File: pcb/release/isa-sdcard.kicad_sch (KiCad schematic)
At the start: 47 parts, among them J1 SDCARD, J2 Bus_ISA_8bit_AB_Rev0, SW1 ADDR SEL, U1 74HC00, U10 74HC74, U11 74HC08, U12 74HC04, U13 74HC74, U2 74HCT32, U3 74HCT139, U4 74HC163, U5 74HC00, U6 74HC165, U7 74HC595, U8 74HCT688, U9 74HCT245, X1 16MHz

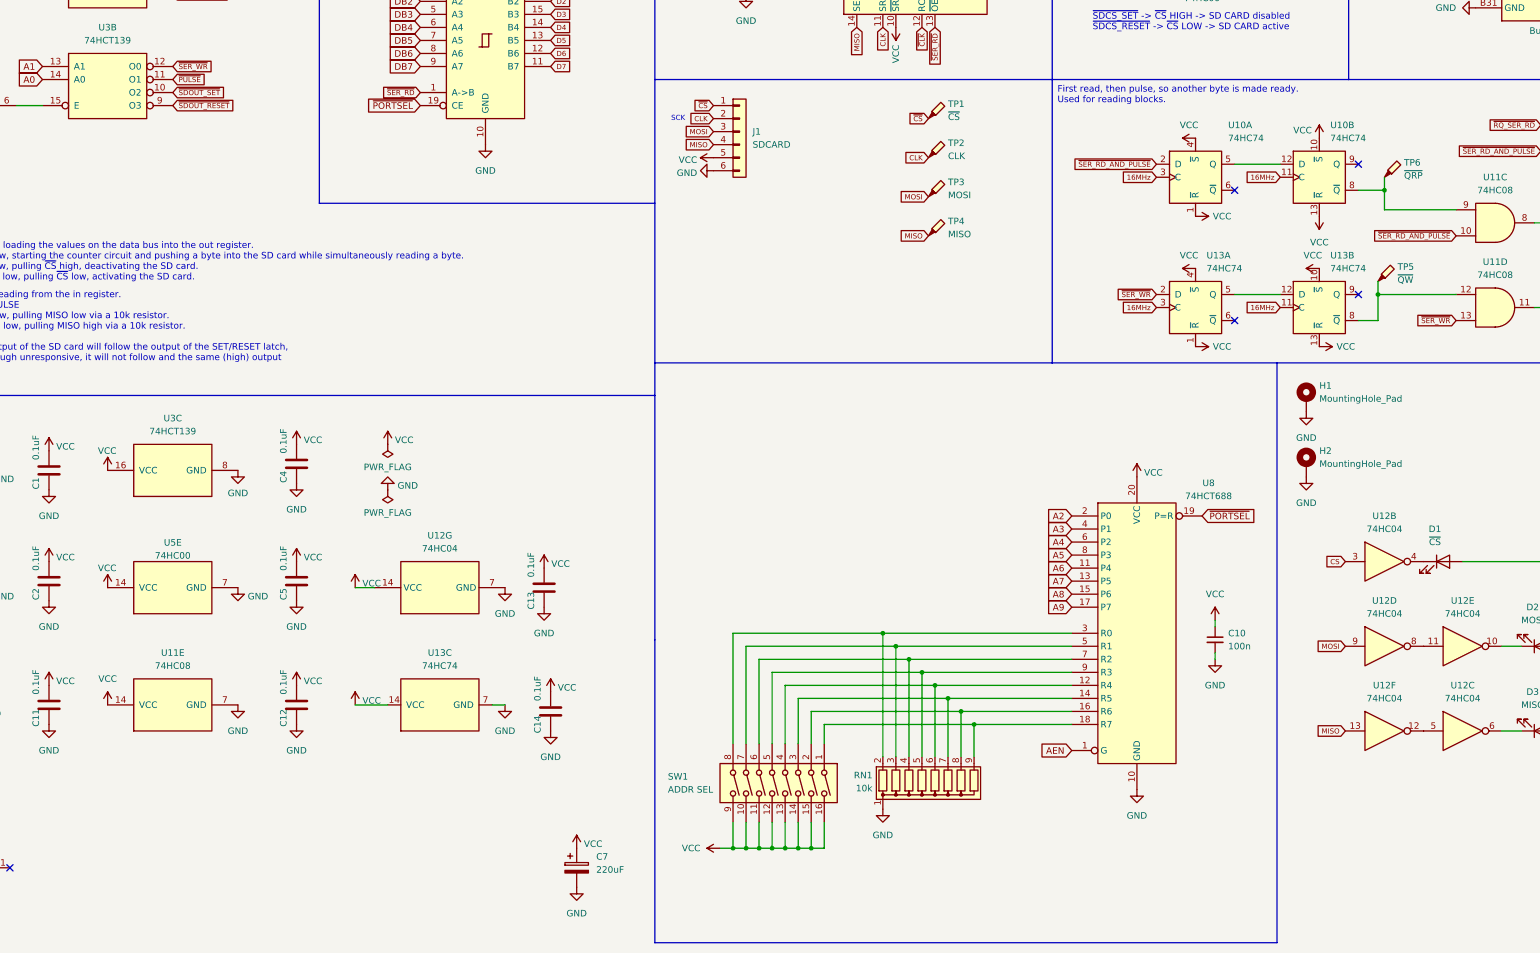
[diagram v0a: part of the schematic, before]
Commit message: Adding PCB variant
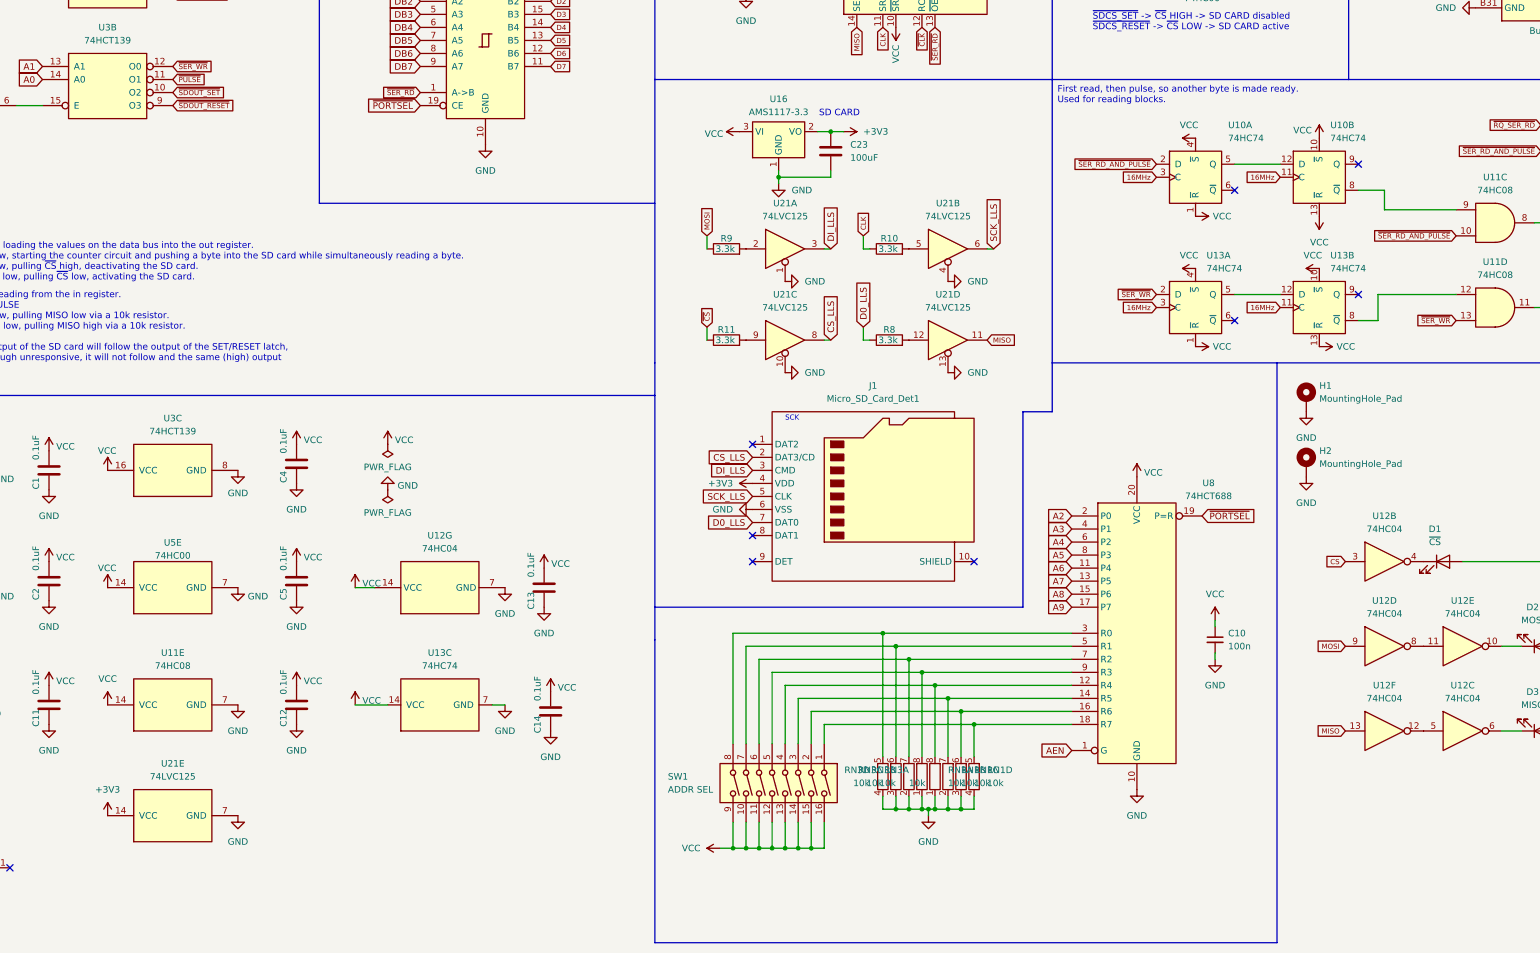
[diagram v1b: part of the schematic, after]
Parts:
- removed C7: 220uF, Capacitor_THT:CP_Radial_D6.3mm_P2.50mm, symbol Device:C_Polarized
- removed J1: SDCARD, sdcard-holder:sdcard-socket, symbol Connector_Generic:Conn_01x06
- removed RN1: 10k, Resistor_THT:R_Array_SIP9, symbol Device:R_Network08
- removed TP1: ~{CS}, TestPoint:TestPoint_Loop_D2.54mm_Drill1.5mm_Beaded, symbol Connector:TestPoint_Probe
- removed TP2: CLK, TestPoint:TestPoint_Loop_D2.54mm_Drill1.5mm_Beaded, symbol Connector:TestPoint_Probe
- removed TP3: MOSI, TestPoint:TestPoint_Loop_D2.54mm_Drill1.5mm_Beaded, symbol Connector:TestPoint_Probe
- removed TP4: MISO, TestPoint:TestPoint_Loop_D2.54mm_Drill1.5mm_Beaded, symbol Connector:TestPoint_Probe
- removed TP5: ~{QW}, TestPoint:TestPoint_Loop_D2.54mm_Drill1.5mm_Beaded, symbol Connector:TestPoint_Probe
- removed TP6: ~{QRP}, TestPoint:TestPoint_Loop_D2.54mm_Drill1.5mm_Beaded, symbol Connector:TestPoint_Probe
- added C23: 100uF, Capacitor_SMD:C_1206_3216Metric_Pad1.33x1.80mm_HandSolder, symbol Device:C
- added J1: Micro_SD_Card_Det1, components:CONN9_MSD-1_CUD, symbol Connector:Micro_SD_Card_Det1
- added R10, R11, R8, R9: 3.3k, Resistor_SMD:R_0805_2012Metric_Pad1.20x1.40mm_HandSolder, symbol Device:R
- added RN1, RN3: 10k, Resistor_SMD:R_Array_Convex_4x0612, symbol Device:R_Pack04_Split
- added U16: AMS1117-3.3, Package_TO_SOT_SMD:SOT-223-3_TabPin2, symbol Regulator_Linear:AMS1117-3.3
- added U21: 74LVC125, Package_SO:TSSOP-14_4.4x5mm_P0.65mm, symbol 74xx:74LVC125
- C1, C10, C11, C12, C13, C14, C2, C3, C4, C5, C6, C8, C9: footprint Capacitor_THT:C_Disc_D5.0mm_W2.5mm_P5.00mm -> Capacitor_SMD:C_0805_2012Metric
- D1, D2, D3: footprint LED_THT:LED_D5.0mm -> LED_SMD:LED_0805_2012Metric
- R1, R2, R3, R4: footprint Resistor_THT:R_Axial_DIN0207_L6.3mm_D2.5mm_P7.62mm_Horizontal -> Resistor_SMD:R_0805_2012Metric
- U1, U10, U11, U12, U13, U2, U5: footprint Package_DIP:DIP-14_W7.62mm_Socket -> Package_SO:SOIC-14_3.9x8.7mm_P1.27mm
- U3, U4, U6, U7: footprint Package_DIP:DIP-16_W7.62mm_Socket -> Package_SO:SOIC-16_3.9x9.9mm_P1.27mm
- U8, U9: footprint Package_DIP:DIP-20_W7.62mm_Socket -> Package_SO:SOIC-20W_7.5x12.8mm_P1.27mm
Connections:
- net CLK: now also R10.1
- net GND: now also C23.2, J1.6 (VSS), RN1.1 (R1.1), RN1.2 (R2.1), RN1.3 (R3.1), RN1.4 (R4.1), RN3.1 (R1.1), RN3.2 (R2.1), RN3.3 (R3.1), RN3.4 (R4.1), U16.1 (GND), U21.1, U21.10, U21.13, U21.4, U21.7 (GND)
- net MISO: now also U21.11
- net MOSI: now also R9.1
- net VCC: now also U16.3 (VI)
- net ~{CS}: now also R11.1
- net at SW1.1, U8.18 (R7): now also RN1.5 (R4.2)
- net at SW1.2, U8.16 (R6): now also RN1.6 (R3.2)
- net at SW1.3, U8.14 (R5): now also RN1.7 (R2.2)
- net at SW1.4, U8.12 (R4): now also RN1.8 (R1.2)
- net at SW1.5, U8.9 (R3): now also RN3.8 (R1.2)
- net at SW1.6, U8.7 (R2): now also RN3.7 (R2.2)
- net at SW1.7, U8.5 (R1): now also RN3.6 (R3.2)
- net at SW1.8, U8.3 (R0): now also RN3.5 (R4.2)
- new net: R11.2, U21.9
- new net: R10.2, U21.5
- new net: R8.2, U21.12
- new net: R9.2, U21.2
- new net +3V3: C23.1, J1.4 (VDD), U16.2 (VO), U21.14 (VCC)
- new net CS_LLS: J1.2 (DAT3/CD), U21.8
- new net D0_LLS: J1.7 (DAT0), R8.1
- new net DI_LLS: J1.3 (CMD), U21.3
- new net SCK_LLS: J1.5 (CLK), U21.6
- no-connect marks 46 -> 50
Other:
- note added: "SD CARD"

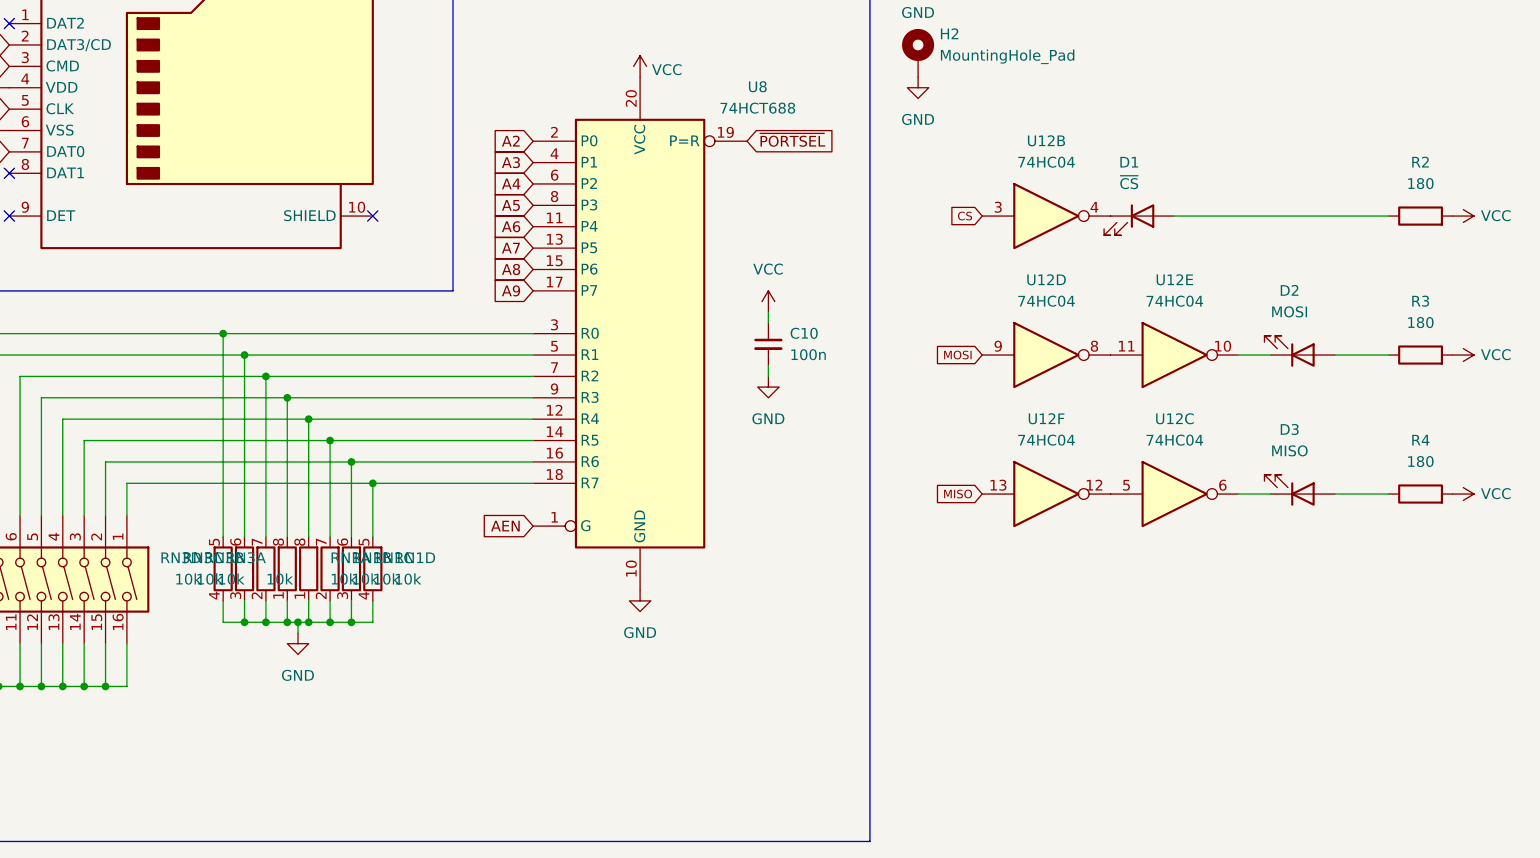
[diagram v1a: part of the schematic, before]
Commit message: Fixing CS bug in code, adding logos to PCB
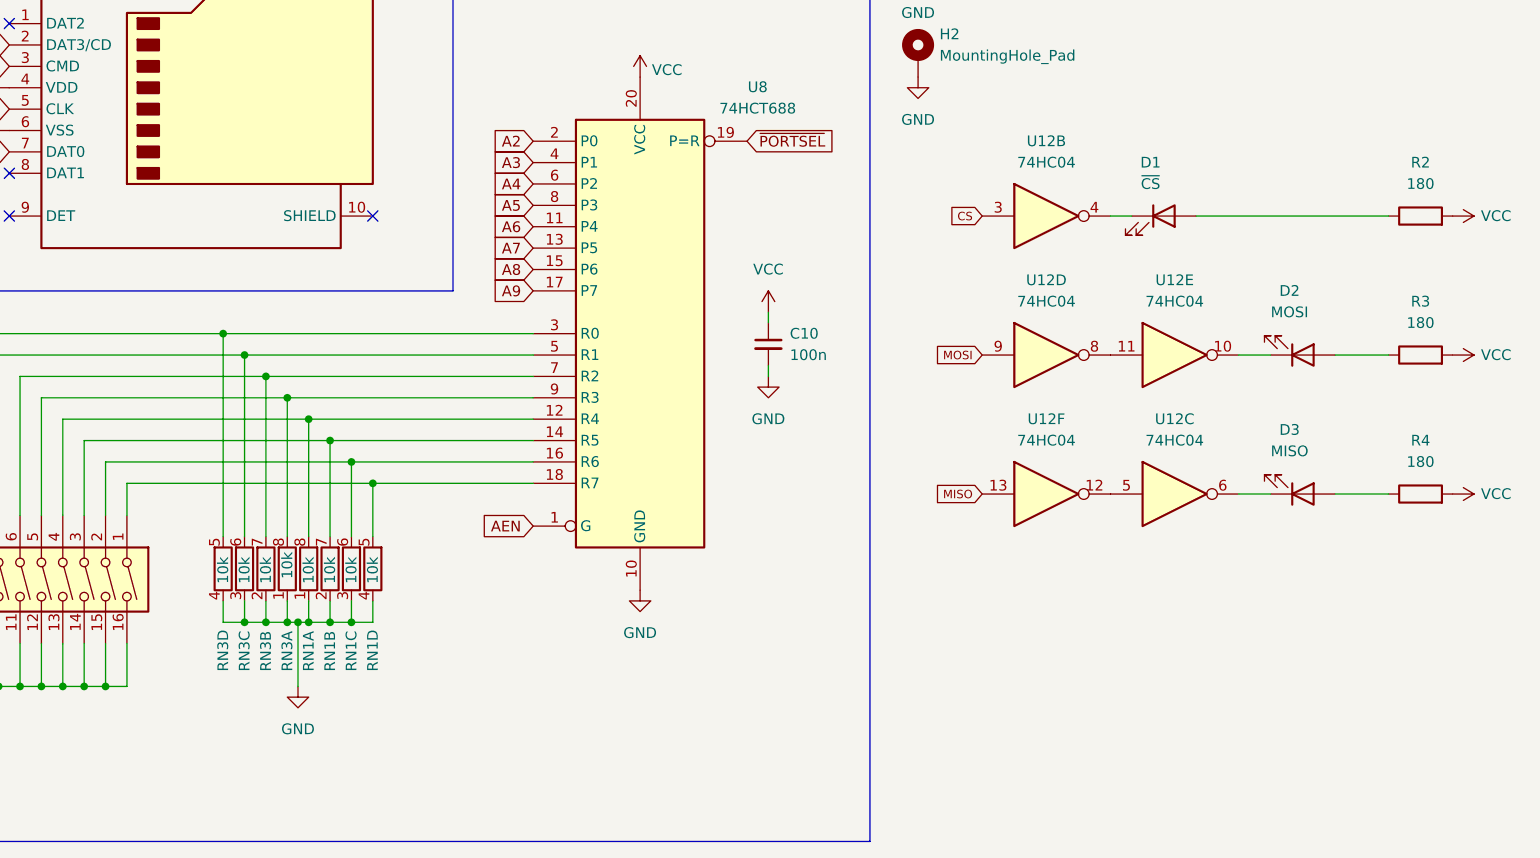
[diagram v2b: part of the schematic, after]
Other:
- moved on the sheet: D1
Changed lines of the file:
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@@
 	(wire
 		(pts
-			(xy 228.6 259.08) (xy 228.6 257.81)
+			(xy 228.6 265.43) (xy 228.6 257.81)
 		)
 		(stroke
@@
 	(wire
 		(pts
+			(xy 327.66 209.55) (xy 325.12 209.55)
+		)
+		(stroke
+			(width 0)
+			(type default)
+		)
+	)
+	(wire
+		(pts
 			(xy 209.55 166.37) (xy 208.28 166.37)
 		)
@@
 	(wire
 		(pts
-			(xy 332.74 209.55) (xy 358.14 209.55)
+			(xy 335.28 209.55) (xy 358.14 209.55)
 		)
 		(stroke
@@
 	(symbol
 		(lib_id "power:GND")
-		(at 228.6 259.08 0)
+		(at 228.6 265.43 0)
 		(unit 1)
 		(exclude_from_sim no)
@@
 		(fields_autoplaced yes)
 		(property "Reference" "#PWR050"
-			(at 228.6 265.43 0)
+			(at 228.6 271.78 0)
 			(effects
 				(font
@@
 		)
 		(property "Value" "GND"
-			(at 228.6 264.16 0)
+			(at 228.6 270.51 0)
 			(effects
 				(font
@@
 		)
 		(property "Footprint" ""
-			(at 228.6 259.08 0)
+			(at 228.6 265.43 0)
 			(effects
 				(font
@@
 		)
 		(property "Datasheet" ""
-			(at 228.6 259.08 0)
+			(at 228.6 265.43 0)
 			(effects
 				(font
@@
 		)
 		(property "Description" "Power symbol creates a global label with name \"GND\" , ground"
-			(at 228.6 259.08 0)
+			(at 228.6 265.43 0)
 			(effects
 				(font
@@
 		(on_board yes)
 		(dnp no)
-		(fields_autoplaced yes)
 		(property "Reference" "RN1"
-			(at 232.41 250.1899 0)
+			(at 229.87 263.652 90)
 			(effects
 				(font
@@
 		)
 		(property "Value" "10k"
-			(at 232.41 252.7299 0)
+			(at 229.87 253.238 90)
 			(effects
 				(font
@@
 	(symbol
 		(lib_id "Device:LED")
-		(at 328.93 209.55 0)
+		(at 331.47 209.55 0)
 		(unit 1)
 		(exclude_from_sim no)
@@
 		(fields_autoplaced yes)
 		(property "Reference" "D1"
-			(at 327.3425 203.2 0)
+			(at 329.8825 203.2 0)
 			(effects
 				(font
@@
 		)
 		(property "Value" "~{CS}"
-			(at 327.3425 205.74 0)
+			(at 329.8825 205.74 0)
 			(effects
 				(font
@@
 		)
 		(property "Footprint" "LED_SMD:LED_0805_2012Metric"
-			(at 328.93 209.55 0)
+			(at 331.47 209.55 0)
 			(effects
 				(font
@@
 		)
 		(property "Datasheet" "~"
-			(at 328.93 209.55 0)
+			(at 331.47 209.55 0)
 			(effects
 				(font
@@
 		)
 		(property "Description" "Light emitting diode"
-			(at 328.93 209.55 0)
+			(at 331.47 209.55 0)
 			(effects
 				(font
@@
 		)
 		(property "Sim.Pins" "1=K 2=A"
-			(at 328.93 209.55 0)
+			(at 331.47 209.55 0)
 			(effects
 				(font
@@
 		(dnp no)
 		(property "Reference" "RN3"
-			(at 224.79 250.1899 0)
+			(at 227.33 263.652 90)
 			(effects
 				(font
@@
 		)
 		(property "Value" "10k"
-			(at 224.79 252.7299 0)
+			(at 227.33 249.428 90)
 			(effects
 				(font
@@
 		(on_board yes)
 		(dnp no)
-		(fields_autoplaced yes)
 		(property "Reference" "RN3"
-			(at 222.25 250.1899 0)
+			(at 224.79 263.652 90)
 			(effects
 				(font
@@
 		)
 		(property "Value" "10k"
-			(at 222.25 252.7299 0)
+			(at 224.79 253.238 90)
 			(effects
 				(font
@@
 		(on_board yes)
 		(dnp no)
-		(fields_autoplaced yes)
 		(property "Reference" "RN3"
-			(at 217.17 250.1899 0)
+			(at 219.71 263.652 90)
 			(effects
 				(font
@@
 		)
 		(property "Value" "10k"
-			(at 217.17 252.7299 0)
+			(at 219.71 253.238 90)
 			(effects
 				(font
@@
 		(on_board yes)
 		(dnp no)
-		(fields_autoplaced yes)
 		(property "Reference" "RN1"
-			(at 240.03 250.1899 0)
+			(at 237.49 263.652 90)
 			(effects
 				(font
@@
 		)
 		(property "Value" "10k"
-			(at 240.03 252.7299 0)
+			(at 237.49 253.238 90)
 			(effects
 				(font
@@
 		(on_board yes)
 		(dnp no)
-		(fields_autoplaced yes)
 		(property "Reference" "RN3"
-			(at 219.71 250.1899 0)
+			(at 222.25 263.652 90)
 			(effects
 				(font
@@
 		)
 		(property "Value" "10k"
-			(at 219.71 252.7299 0)
+			(at 222.25 253.238 90)
 			(effects
 				(font
@@
 		(on_board yes)
 		(dnp no)
-		(fields_autoplaced yes)
 		(property "Reference" "RN1"
-			(at 234.95 250.1899 0)
+			(at 232.41 263.652 90)
 			(effects
 				(font
@@
 		)
 		(property "Value" "10k"
-			(at 234.95 252.7299 0)
+			(at 232.41 253.238 90)
 			(effects
 				(font
@@
 		(on_board yes)
 		(dnp no)
-		(fields_autoplaced yes)
 		(property "Reference" "RN1"
-			(at 237.49 250.1899 0)
+			(at 234.95 263.652 90)
 			(effects
 				(font
@@
 		)
 		(property "Value" "10k"
-			(at 237.49 252.7299 0)
+			(at 234.95 253.238 90)
 			(effects
 				(font
